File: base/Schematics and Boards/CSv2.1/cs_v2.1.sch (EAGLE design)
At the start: 77 parts, among them J101 J-JTAG-CORTEX-NEEDLE6-LEGS, J301 HIROSE-DF40_50-PIN_CONNECTORS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, J302 HIROSE-DF40_50-PIN_CONNECTORS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, Q1 DMG3415UFY4Q-7F, U1 NCP708MU330TAG, U101 ATSAMD51, U2 W25N01GVZEIG, U201 COULOMB-MAX17262, U202 MAX77827BEWC+T, U203 SENSOR-SI7006, U204 LOADSWITCH-MIC94164, U205 LOADSWITCH-MIC94164, U3 TS3A24159YZPR, U4 LOADSWITCH-MIC94164, U5 PD3S140-7, Y102 ABS07-32.768KHZ-9-T

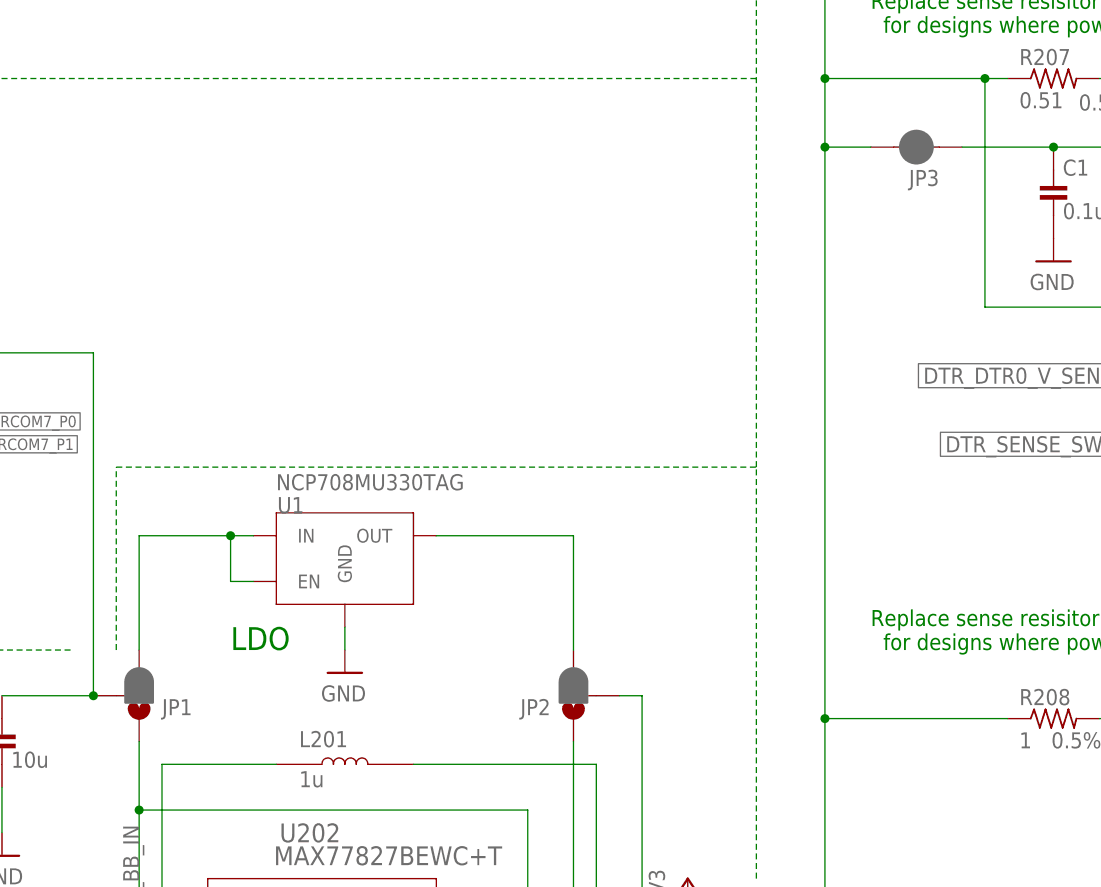
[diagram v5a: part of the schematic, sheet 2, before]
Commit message: CSv2.1 main board part placement; routing for power traces
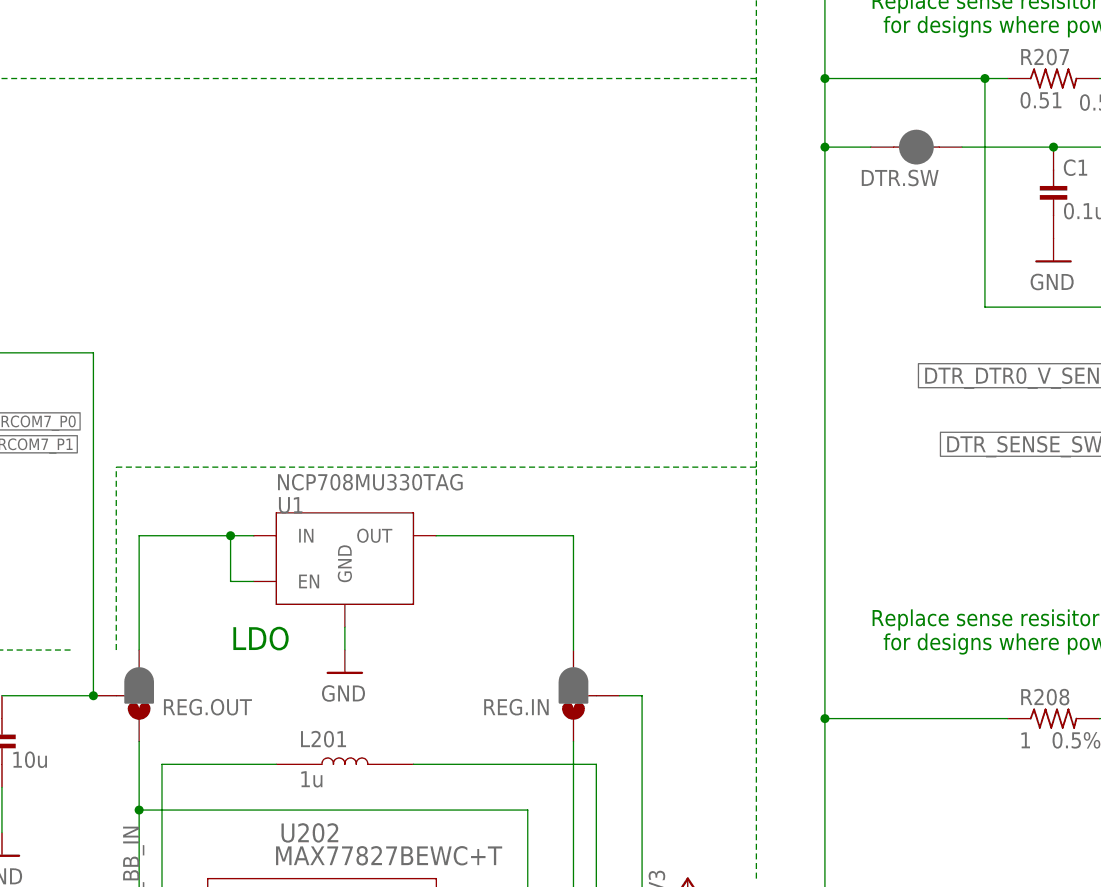
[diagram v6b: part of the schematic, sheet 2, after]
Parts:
- renumbered JP1 to REG.OUT, JP2 to REG.IN, JP3 to DTR.SW
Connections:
- net N$15 renamed LDO_REG_OUT
- net N$3 renamed BB_REG_OUT
- net N$7 renamed REG_LDO_IN
- net VREG_LX1 renamed BB_LX1
- net VREG_LX2 renamed BB_LX2
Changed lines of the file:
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@@
 <attribute name="PART_NO" value="LQH3NPN100MMEL"/>
 </part>
-<part name="JP1" library="SparkFun-Jumpers" deviceset="JUMPER-SMT_3_1-NC_PASTE" device="_NO-SILK" package3d_urn="urn:adsk.eagle:package:39291/1"/>
-<part name="JP2" library="SparkFun-Jumpers" deviceset="JUMPER-SMT_3_1-NC_PASTE" device="_NO-SILK" package3d_urn="urn:adsk.eagle:package:39291/1"/>
+<part name="REG.OUT" library="SparkFun-Jumpers" deviceset="JUMPER-SMT_3_1-NC_PASTE" device="_NO-SILK" package3d_urn="urn:adsk.eagle:package:39291/1"/>
+<part name="REG.IN" library="SparkFun-Jumpers" deviceset="JUMPER-SMT_3_1-NC_PASTE" device="_NO-SILK" package3d_urn="urn:adsk.eagle:package:39291/1"/>
 <part name="GND6" library="Supplies" deviceset="GND" device=""/>
 <part name="U1" library="Regulators" deviceset="LDO_ONSEMI_NCP708" device="" value="NCP708MU330TAG"/>
@@
 <attribute name="SPICEPREFIX" value="G"/>
 </part>
-<part name="JP3" library="Connectors" deviceset="JUMPER-SMT_2_NC_PASTE" device="_NO-SILK" package3d_urn="urn:adsk.eagle:package:39283/1"/>
+<part name="DTR.SW" library="Connectors" deviceset="JUMPER-SMT_2_NC_PASTE" device="_NO-SILK" package3d_urn="urn:adsk.eagle:package:39283/1"/>
 <part name="JP7" library="Connectors" deviceset="JUMPER-SMT_2_NC_PASTE" device="_NO-SILK" package3d_urn="urn:adsk.eagle:package:39283/1"/>
 <part name="U4" library="Switches" deviceset="LOADSWITCH-MIC9416" device="" technology="4" value="LOADSWITCH-MIC94164">
@@
 <attribute name="NAME" x="374.396" y="133.35" size="1.778" layer="95" rot="MR90"/>
 </instance>
-<instance part="JP1" gate="G$1" x="187.96" y="134.62" smashed="yes" rot="MR180">
+<instance part="REG.OUT" gate="G$1" x="187.96" y="134.62" smashed="yes" rot="MR180">
 <attribute name="NAME" x="190.5" y="134.239" size="1.778" layer="95" font="vector" rot="MR180"/>
 </instance>
-<instance part="JP2" gate="G$1" x="236.22" y="134.62" smashed="yes" rot="R180">
+<instance part="REG.IN" gate="G$1" x="236.22" y="134.62" smashed="yes" rot="R180">
 <attribute name="NAME" x="233.68" y="134.239" size="1.778" layer="95" font="vector" rot="R180"/>
 </instance>
@@
 <attribute name="VALUE" x="319.913" y="144.145" size="1.778" layer="96"/>
 </instance>
-<instance part="JP3" gate="G$1" x="274.32" y="195.58" smashed="yes" rot="R180">
+<instance part="DTR.SW" gate="G$1" x="274.32" y="195.58" smashed="yes" rot="R180">
 <attribute name="NAME" x="276.86" y="193.04" size="1.778" layer="95" font="vector" rot="R180"/>
 </instance>
@@
 </segment>
 </net>
-<net name="VREG_LX1" class="0">
+<net name="BB_LX1" class="0">
 <segment>
 <pinref part="U202" gate="A" pin="LX1"/>
@@
 </segment>
 </net>
-<net name="VREG_LX2" class="0">
+<net name="BB_LX2" class="0">
 <segment>
 <pinref part="L201" gate="&gt;NAME" pin="2"/>
@@
 <wire x1="243.84" y1="106.68" x2="248.92" y2="106.68" width="0.1524" layer="91"/>
 <junction x="281.94" y="203.2"/>
-<pinref part="JP2" gate="G$1" pin="2"/>
+<pinref part="REG.IN" gate="G$1" pin="2"/>
 <wire x1="241.3" y1="134.62" x2="243.84" y2="134.62" width="0.1524" layer="91"/>
 <junction x="264.16" y="195.58"/>
@@
 <junction x="304.8" y="91.44"/>
 <wire x1="264.16" y1="195.58" x2="269.24" y2="195.58" width="0.1524" layer="91"/>
-<pinref part="JP3" gate="G$1" pin="2"/>
+<pinref part="DTR.SW" gate="G$1" pin="2"/>
 </segment>
 </net>
@@
 <wire x1="172.72" y1="134.62" x2="182.88" y2="134.62" width="0.1524" layer="91"/>
 <junction x="182.88" y="134.62"/>
-<pinref part="JP1" gate="G$1" pin="2"/>
+<pinref part="REG.OUT" gate="G$1" pin="2"/>
 </segment>
 </net>
@@
 <wire x1="190.5" y1="106.68" x2="187.96" y2="106.68" width="0.1524" layer="91"/>
 <label x="187.96" y="106.68" size="1.778" layer="95" rot="R90"/>
-<pinref part="JP1" gate="G$1" pin="1"/>
+<pinref part="REG.OUT" gate="G$1" pin="1"/>
 <wire x1="187.96" y1="106.68" x2="187.96" y2="121.92" width="0.1524" layer="91"/>
 <wire x1="187.96" y1="121.92" x2="187.96" y2="129.54" width="0.1524" layer="91"/>
@@
 </segment>
 </net>
-<net name="N$3" class="1">
+<net name="BB_REG_OUT" class="1">
 <segment>
 <pinref part="U202" gate="A" pin="OUT"/>
@@
 <junction x="231.14" y="106.68"/>
 <wire x1="231.14" y1="106.68" x2="236.22" y2="106.68" width="0.1524" layer="91"/>
-<pinref part="JP2" gate="G$1" pin="1"/>
+<pinref part="REG.IN" gate="G$1" pin="1"/>
 <wire x1="236.22" y1="129.54" x2="236.22" y2="106.68" width="0.1524" layer="91"/>
 </segment>
 </net>
-<net name="N$7" class="0">
+<net name="REG_LDO_IN" class="0">
 <segment>
 <pinref part="U1" gate="G$1" pin="IN"/>
@@
 <wire x1="198.12" y1="147.32" x2="198.12" y2="152.4" width="0.1524" layer="91"/>
 <junction x="198.12" y="152.4"/>
-<pinref part="JP1" gate="G$1" pin="3"/>
+<pinref part="REG.OUT" gate="G$1" pin="3"/>
 <wire x1="187.96" y1="139.7" x2="187.96" y2="152.4" width="0.1524" layer="91"/>
 </segment>
 </net>
-<net name="N$15" class="0">
+<net name="LDO_REG_OUT" class="0">
 <segment>
 <pinref part="U1" gate="G$1" pin="OUT"/>
 <wire x1="220.98" y1="152.4" x2="236.22" y2="152.4" width="0.1524" layer="91"/>
-<pinref part="JP2" gate="G$1" pin="3"/>
+<pinref part="REG.IN" gate="G$1" pin="3"/>
 <wire x1="236.22" y1="152.4" x2="236.22" y2="139.7" width="0.1524" layer="91"/>
 </segment>
@@
 <wire x1="289.56" y1="195.58" x2="322.58" y2="195.58" width="0.1524" layer="91"/>
 <wire x1="322.58" y1="195.58" x2="322.58" y2="187.96" width="0.1524" layer="91"/>
-<pinref part="JP3" gate="G$1" pin="1"/>
-</segment>
-</net>
+<pinref part="DTR.SW" gate="G$1" pin="1"/>
+</segment>
+</net>

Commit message: Gerbers, BOM, and minor part changes
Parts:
- C114: MP (none) -> C0402C105M8PACTU; MPN (none) -> C0402C105M8PACTU
- C204: MP (none) -> C0402C105M8PACTU; MPN (none) -> C0402C105M8PACTU; PART_NO C0402C105K8PACTU -> C0402C105M8PACTU
- J301: MP (none) -> DF40HC(4.0)-50DS-0.4V(51); MPN (none) -> DF40HC(4.0)-50DS-0.4V(51)
- J302: MP (none) -> DF40HC(4.0)-50DS-0.4V(51); MPN (none) -> DF40HC(4.0)-50DS-0.4V(51); PART_NO DF40HC(4.0)-50DS-0.4V(58) -> DF40HC(4.0)-50DS-0.4V(51)
- L201: device Inductors:L1008 -> Inductors:XAL40; PART_NO CIGT252010EH1R0MNE -> XAL4020-102MEC
- Q1: MP (none) -> DMG3415U-7; MPN (none) -> DMG3415U-7; PART_NO (none) -> DMG3415U-7
- U3: MP (none) -> TS3A24159YZPR; MPN (none) -> TS3A24159YZPR; PART_NO (none) -> TS3A24159YZPR
- renumbered JP7 to JP.PROC
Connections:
- net BB_LX1: now also L201.2; no longer L201.1
- net BB_LX2: now also L201.1; no longer L201.2
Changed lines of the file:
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@@
 <part name="+3V2" library="Supplies" deviceset="+3V3" device=""/>
 <part name="C114" library="Capacitors" deviceset="C-" device="0402" value="1u">
+<attribute name="MP" value="C0402C105M8PACTU"/>
+<attribute name="MPN" value="C0402C105M8PACTU"/>
 <attribute name="PART_NO" value="C0402C105M8PACTU"/>
 <attribute name="TC" value="X5R"/>
@@
 </part>
 <part name="C204" library="Capacitors" deviceset="C-" device="0402" value="1u">
-<attribute name="PART_NO" value="C0402C105K8PACTU"/>
+<attribute name="MP" value="C0402C105M8PACTU"/>
+<attribute name="MPN" value="C0402C105M8PACTU"/>
+<attribute name="PART_NO" value="C0402C105M8PACTU"/>
 <attribute name="TC" value="X5R"/>
 <attribute name="VOLTAGE" value="10V"/>
 </part>
-<part name="L201" library="Inductors" deviceset="L1008" device="" value="1u">
-<attribute name="PART_NO" value="CIGT252010EH1R0MNE"/>
+<part name="L201" library="Inductors" deviceset="XAL40" device="" value="1u">
+<attribute name="PART_NO" value="XAL4020-102MEC"/>
 </part>
 <part name="GND12" library="Supplies" deviceset="GND" device=""/>
@@
 <part name="BORDER301" library="Graphics" deviceset="BORDER-CMU" device=""/>
 <part name="J301" library="Connectors" deviceset="HIROSE-DF40_50-PIN_CONNECTORS" device="-RECEPTACLE">
+<attribute name="MP" value="DF40HC(4.0)-50DS-0.4V(51)"/>
+<attribute name="MPN" value="DF40HC(4.0)-50DS-0.4V(51)"/>
 <attribute name="PART_NO" value="DF40HC(4.0)-50DS-0.4V(51)"/>
 </part>
@@
 <part name="+3V8" library="Supplies" deviceset="+3V3" device=""/>
 <part name="J302" library="Connectors" deviceset="HIROSE-DF40_50-PIN_CONNECTORS" device="-RECEPTACLE" value="HIROSE-DF40_50-PIN_CONNECTORS-RECEPTACLE">
-<attribute name="PART_NO" value="DF40HC(4.0)-50DS-0.4V(58)"/>
+<attribute name="MP" value="DF40HC(4.0)-50DS-0.4V(51)"/>
+<attribute name="MPN" value="DF40HC(4.0)-50DS-0.4V(51)"/>
+<attribute name="PART_NO" value="DF40HC(4.0)-50DS-0.4V(51)"/>
 </part>
 <part name="GND22" library="Supplies" deviceset="GND" device=""/>
@@
 <part name="U1" library="Regulators" deviceset="LDO_ONSEMI_NCP708" device="" value="NCP708MU330TAG"/>
 <part name="U2" library="Storage" deviceset="W25N01GVZEIG" device=""/>
-<part name="U3" library="Switches" deviceset="TS3A24159YZPR" device=""/>
+<part name="U3" library="Switches" deviceset="TS3A24159YZPR" device="">
+<attribute name="MP" value="TS3A24159YZPR"/>
+<attribute name="MPN" value="TS3A24159YZPR"/>
+<attribute name="PART_NO" value="TS3A24159YZPR"/>
+</part>
 <part name="C1" library="Capacitors" deviceset="C-" device="0402" value="0.1u">
 <attribute name="PART_NO" value="C0402C104K8RACTU"/>
@@
 </part>
 <part name="DTR.SW" library="Connectors" deviceset="JUMPER-SMT_2_NC_PASTE" device="_NO-SILK" package3d_urn="urn:adsk.eagle:package:39283/1"/>
-<part name="JP7" library="Connectors" deviceset="JUMPER-SMT_2_NC_PASTE" device="_NO-SILK" package3d_urn="urn:adsk.eagle:package:39283/1"/>
+<part name="JP.PROC" library="Connectors" deviceset="JUMPER-SMT_2_NC_PASTE" device="_NO-SILK" package3d_urn="urn:adsk.eagle:package:39283/1"/>
 <part name="U4" library="Switches" deviceset="LOADSWITCH-MIC9416" device="" technology="4" value="LOADSWITCH-MIC94164">
 <attribute name="PART_NO" value="MIC94164YCS-TR"/>
@@
 </part>
 <part name="GND16" library="Supplies" deviceset="GND" device=""/>
-<part name="Q1" library="Switches" deviceset="DMG3415UFY4Q-7" device="F"/>
+<part name="Q1" library="Switches" deviceset="DMG3415UFY4Q-7" device="F">
+<attribute name="MP" value="DMG3415U-7"/>
+<attribute name="MPN" value="DMG3415U-7"/>
+<attribute name="PART_NO" value="DMG3415U-7"/>
+</part>
 </parts>
 <sheets>
@@
 <attribute name="VALUE" x="272.796" y="149.479" size="1.778" layer="96"/>
 <attribute name="PART_NO" x="271.78" y="152.4" size="1.778" layer="96" display="off"/>
+<attribute name="MP" x="271.78" y="152.4" size="1.778" layer="96" display="off"/>
+<attribute name="MPN" x="271.78" y="152.4" size="1.778" layer="96" display="off"/>
 </instance>
 <instance part="C101" gate="G$1" x="190.5" y="198.12" smashed="yes">
@@
 <attribute name="VALUE" x="166.116" y="96.139" size="1.778" layer="96"/>
 <attribute name="PART_NO" x="165.1" y="99.06" size="1.778" layer="96" display="off"/>
-</instance>
-<instance part="L201" gate="&gt;NAME" x="210.82" y="127" smashed="yes">
-<attribute name="NAME" x="205.73153125" y="128.90818125" size="1.780959375" layer="95"/>
-<attribute name="VALUE" x="205.734559375" y="124.45728125" size="1.779909375" layer="96"/>
-<attribute name="PART_NO" x="210.82" y="127" size="1.778" layer="96" display="off"/>
+<attribute name="MP" x="165.1" y="99.06" size="1.778" layer="96" display="off"/>
+<attribute name="MPN" x="165.1" y="99.06" size="1.778" layer="96" display="off"/>
+</instance>
+<instance part="L201" gate="G$1" x="210.82" y="127" smashed="yes" rot="R270">
+<attribute name="NAME" x="212.72818125" y="132.08846875" size="1.780959375" layer="95" rot="R270"/>
+<attribute name="VALUE" x="208.27728125" y="132.085440625" size="1.779909375" layer="96" rot="R270"/>
+<attribute name="PART_NO" x="210.82" y="127" size="1.778" layer="96" rot="R270" display="off"/>
 </instance>
 <instance part="GND12" gate="1" x="177.8" y="86.36" smashed="yes">
@@
 <attribute name="NAME" x="312.7756" y="186.9186" size="2.0828" layer="95" ratio="6" rot="SR0"/>
 <attribute name="VALUE" x="307.0606" y="184.3786" size="2.0828" layer="96" ratio="6" rot="SR0"/>
+<attribute name="MP" x="322.58" y="167.64" size="1.778" layer="96" display="off"/>
+<attribute name="MPN" x="322.58" y="167.64" size="1.778" layer="96" display="off"/>
+<attribute name="PART_NO" x="322.58" y="167.64" size="1.778" layer="96" display="off"/>
 </instance>
 <instance part="C1" gate="G$1" x="289.56" y="190.5" smashed="yes">
@@
 <attribute name="NAME" x="276.86" y="193.04" size="1.778" layer="95" font="vector" rot="R180"/>
 </instance>
-<instance part="JP7" gate="G$1" x="347.98" y="218.44" smashed="yes" rot="R180">
+<instance part="JP.PROC" gate="G$1" x="347.98" y="218.44" smashed="yes" rot="R180">
 <attribute name="NAME" x="350.52" y="215.9" size="1.778" layer="95" font="vector" rot="R180"/>
 </instance>
@@
 <attribute name="VALUE" x="41.91" y="212.09" size="1.778" layer="96"/>
 <attribute name="NAME" x="59.69" y="214.63" size="1.778" layer="95"/>
+<attribute name="MP" x="66.04" y="213.36" size="1.778" layer="96" display="off"/>
+<attribute name="MPN" x="66.04" y="213.36" size="1.778" layer="96" display="off"/>
+<attribute name="PART_NO" x="66.04" y="213.36" size="1.778" layer="96" display="off"/>
 </instance>
 </instances>
@@
 <pinref part="U202" gate="A" pin="LX1"/>
 <wire x1="190.5" y1="109.22" x2="190.5" y2="127" width="0.1524" layer="91"/>
-<pinref part="L201" gate="&gt;NAME" pin="1"/>
-<wire x1="190.5" y1="127" x2="203.2" y2="127" width="0.1524" layer="91"/>
+<pinref part="L201" gate="G$1" pin="2"/>
+<wire x1="190.5" y1="127" x2="205.74" y2="127" width="0.1524" layer="91"/>
 </segment>
 </net>
 <net name="BB_LX2" class="0">
 <segment>
-<pinref part="L201" gate="&gt;NAME" pin="2"/>
-<wire x1="218.44" y1="127" x2="238.76" y2="127" width="0.1524" layer="91"/>
 <wire x1="238.76" y1="127" x2="238.76" y2="101.6" width="0.1524" layer="91"/>
 <pinref part="U202" gate="A" pin="LX2"/>
 <wire x1="238.76" y1="101.6" x2="226.06" y2="101.6" width="0.1524" layer="91"/>
+<pinref part="L201" gate="G$1" pin="1"/>
+<wire x1="238.76" y1="127" x2="215.9" y2="127" width="0.1524" layer="91"/>
 </segment>
 </net>
@@
 <wire x1="383.54" y1="218.44" x2="386.08" y2="220.98" width="0.1524" layer="91"/>
 <wire x1="353.06" y1="218.44" x2="383.54" y2="218.44" width="0.1524" layer="91"/>
-<pinref part="JP7" gate="G$1" pin="1"/>
+<pinref part="JP.PROC" gate="G$1" pin="1"/>
 </segment>
 <segment>
@@
 <pinref part="R206" gate="G$1" pin="2"/>
 <wire x1="294.64" y1="218.44" x2="342.9" y2="218.44" width="0.1524" layer="91"/>
-<pinref part="JP7" gate="G$1" pin="2"/>
+<pinref part="JP.PROC" gate="G$1" pin="2"/>
 <label x="309.88" y="218.44" size="1.778" layer="95"/>
 </segment>
@@
 <attribute name="NAME" x="80.4966" y="142.21801875" size="1.273659375" layer="95" rot="R90"/>
 <attribute name="PART_NO" x="114.3" y="149.86" size="1.778" layer="96" rot="R90" display="off"/>
+<attribute name="MP" x="114.3" y="149.86" size="1.778" layer="96" rot="R90" display="off"/>
+<attribute name="MPN" x="114.3" y="149.86" size="1.778" layer="96" rot="R90" display="off"/>
 </instance>
 <instance part="J302" gate="G$1" x="289.56" y="149.86" smashed="yes" rot="R90">
 <attribute name="NAME" x="265.9166" y="142.21801875" size="1.273659375" layer="95" rot="R90"/>
 <attribute name="PART_NO" x="289.56" y="149.86" size="1.778" layer="96" rot="R90" display="off"/>
+<attribute name="MPN" x="289.56" y="149.86" size="1.778" layer="96" rot="R90" display="off"/>
+<attribute name="MP" x="289.56" y="149.86" size="1.778" layer="96" rot="R90" display="off"/>
 </instance>
 <instance part="GND22" gate="1" x="86.36" y="127" smashed="yes">

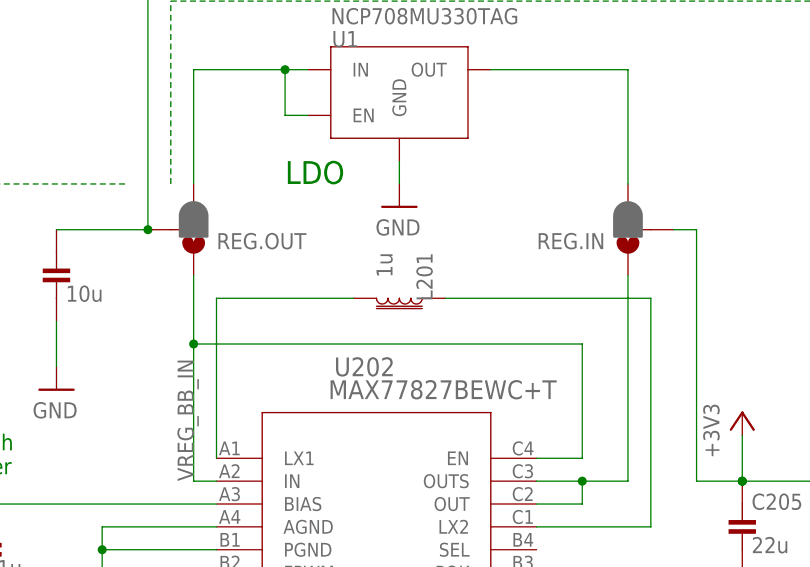
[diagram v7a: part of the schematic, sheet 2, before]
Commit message: DBG: Replace bias resistors of current measurement w/ correct part
And regenerate the CAM files.
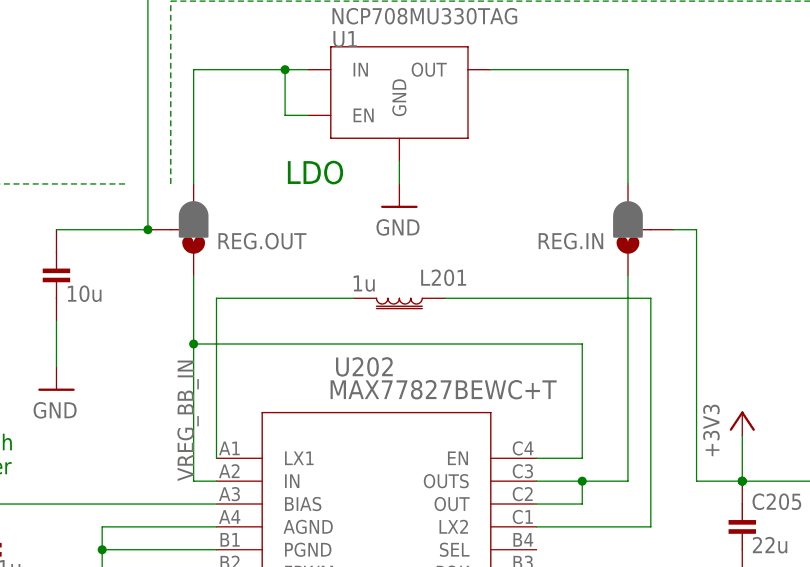
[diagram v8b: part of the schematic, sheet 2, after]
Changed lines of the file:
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@@
 </instance>
 <instance part="L201" gate="G$1" x="210.82" y="127" smashed="yes" rot="R270">
-<attribute name="NAME" x="212.72818125" y="132.08846875" size="1.780959375" layer="95" rot="R270"/>
-<attribute name="VALUE" x="208.27728125" y="132.085440625" size="1.779909375" layer="96" rot="R270"/>
+<attribute name="NAME" x="218.44846875" y="130.17181875" size="1.780959375" layer="95" rot="R180"/>
+<attribute name="VALUE" x="208.285440625" y="129.54271875" size="1.779909375" layer="96" rot="R180"/>
 <attribute name="PART_NO" x="210.82" y="127" size="1.778" layer="96" rot="R270" display="off"/>
 </instance>
